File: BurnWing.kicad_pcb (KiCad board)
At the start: 2 copper layers, 50.8 x 22.9 mm, 31 parts, among them J1 Molex_PicoBlade_53398-0471_1x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, J2 Molex_PicoBlade_53047-0610_1x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, J3 feather long, J4 feather short, U1 BTS3405GXUMA1

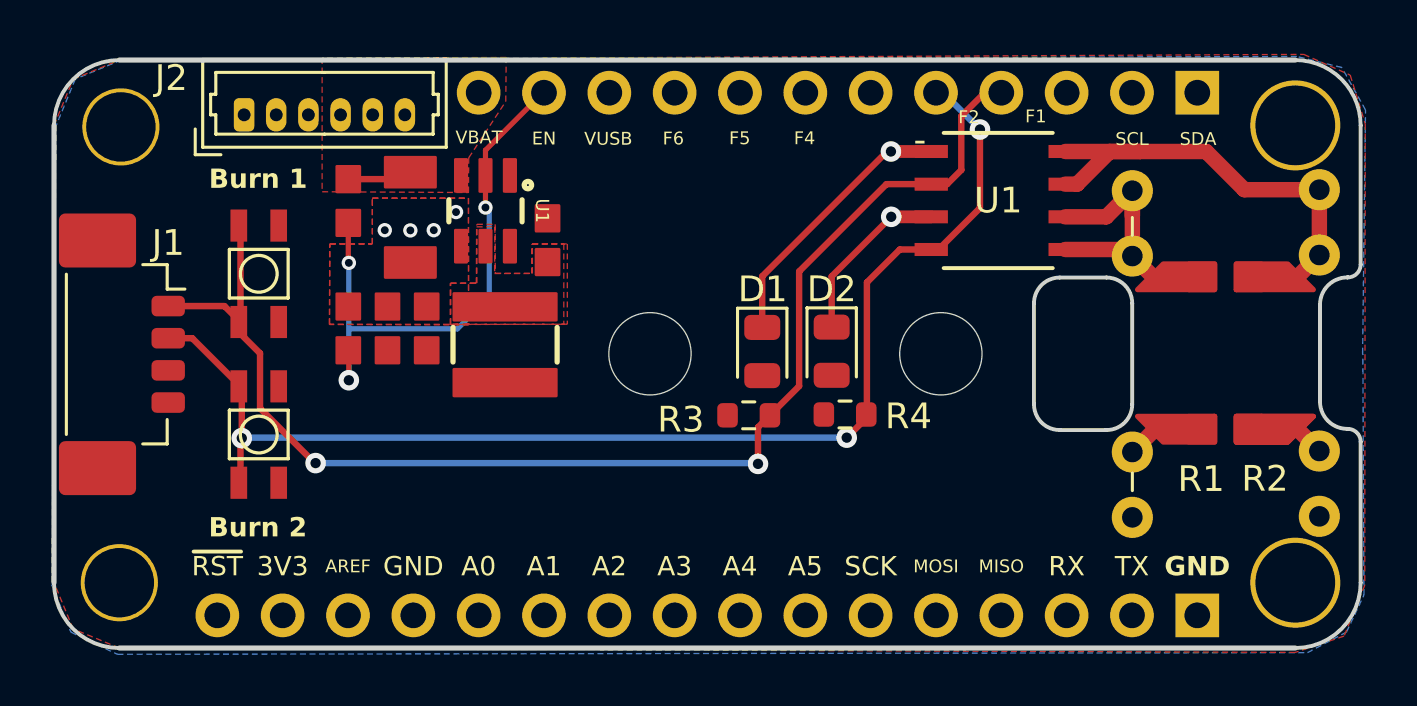
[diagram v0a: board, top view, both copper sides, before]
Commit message: Layout adjustments + added diodes
Added some diodes to prevent backfeeding of test voltage.

Routed remaining two picoblade pins to EN pin on buck reg.
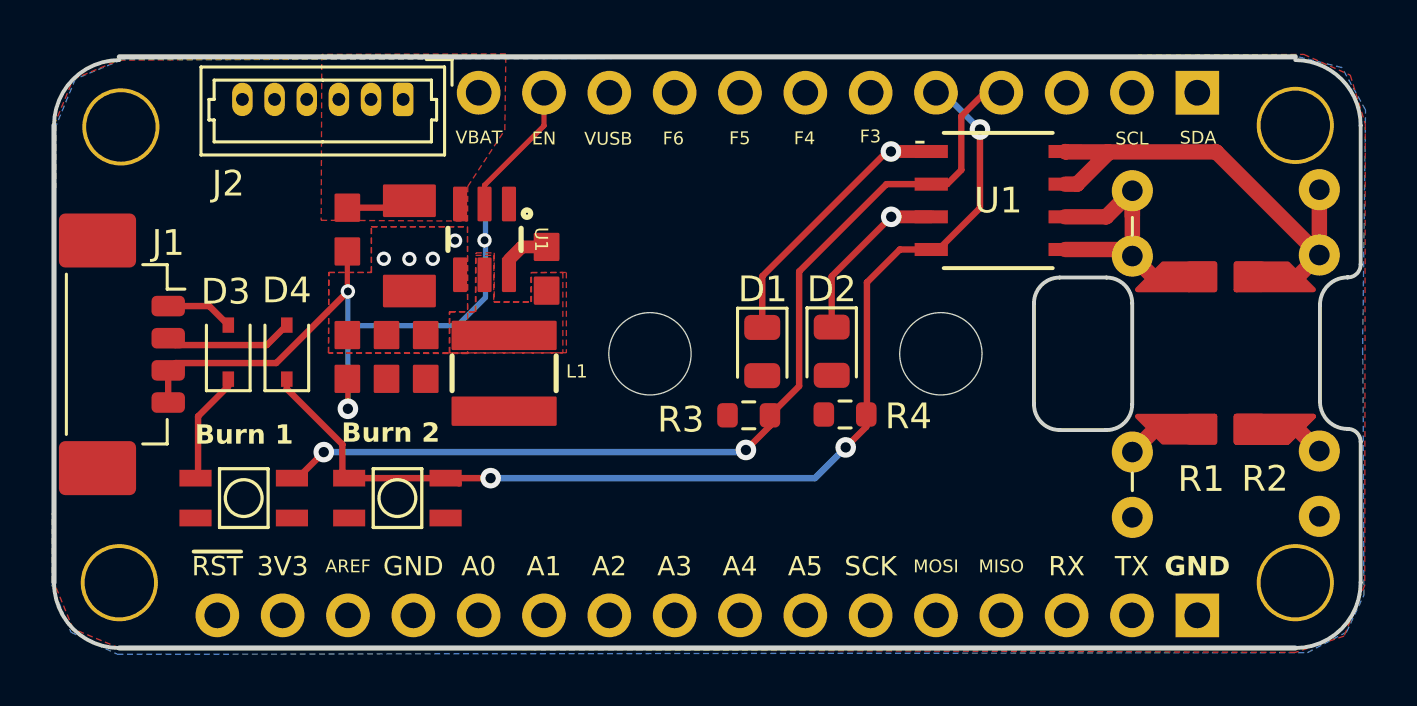
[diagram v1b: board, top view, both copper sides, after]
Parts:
- removed the REF** at (173.7, 105.7)
- removed the REF** at (173.7, 87.9)
- added D3: D_Schottky_Small, Diode_SMD:D_SOD-323, F.Cu at (132.2, 96.8)
- added D4: D_Schottky_Small, Diode_SMD:D_SOD-323, F.Cu at (134.4, 96.8)
- added REF**: MountingHole_2.6mm_M2.5, MountingHole:MountingHole_2.7mm_M2.5, F.Cu at (173.7, 105.7)
- added REF**: MountingHole_2.6mm_M2.5, MountingHole:MountingHole_2.7mm_M2.5, F.Cu at (173.7, 87.9)
- moved Burn 1 8.74 mm to (132.8, 102.4), turned to 180 degrees
- moved J2 6.21 mm to (139.0, 86.9), turned to 180 degrees
- moved Burn 2 5.93 mm to (138.8, 102.4), turned to 180 degrees
- moved C2 1.11 mm to (144.6, 93.5)
- moved C3 1.11 mm to (138.3, 96.9)
- moved C4 1.11 mm to (139.9, 96.9)
- moved R1 1.11 mm to (136.8, 92.0)
- moved R2 1.11 mm to (136.8, 96.9)
- moved U1 1.11 mm to (142.1, 92.4)
- moved C1 1.11 mm to (139.2, 92.6)
- moved L1 1.11 mm to (142.9, 97.6)
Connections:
- J1 pad 3: unconnected-(J1-Pad3) -> EN3V
- J1 pad 4: unconnected-(J1-Pad4) -> EN3V
- J2 pad 1: GND -> Vin
- J2 pad 2: GND -> Vin
- J2 pad 3: GND -> Vin
- J2 pad 4: Vin -> GND
- J2 pad 5: Vin -> GND
- J2 pad 6: Vin -> GND
- U1 pad 6: Net-(R4-Pad2) -> (no net)
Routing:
- net EN3V: track 22.1 -> 31.6 mm
- net IN1: track 51.0 -> 44.9 mm
- net (no net): track 0.00 -> 2.25 mm
- net IN2: track 49.7 -> 48.9 mm
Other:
- board size 50.8 x 22.9 mm -> 50.8 x 23 mm
- board text added: "F3"
- board text removed: "F1"
- board text removed: "F2"
- board text removed: "MountingHole_2.7mm_M2.5"

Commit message: Added couple missing traces
Added missing traces and updated pics/step
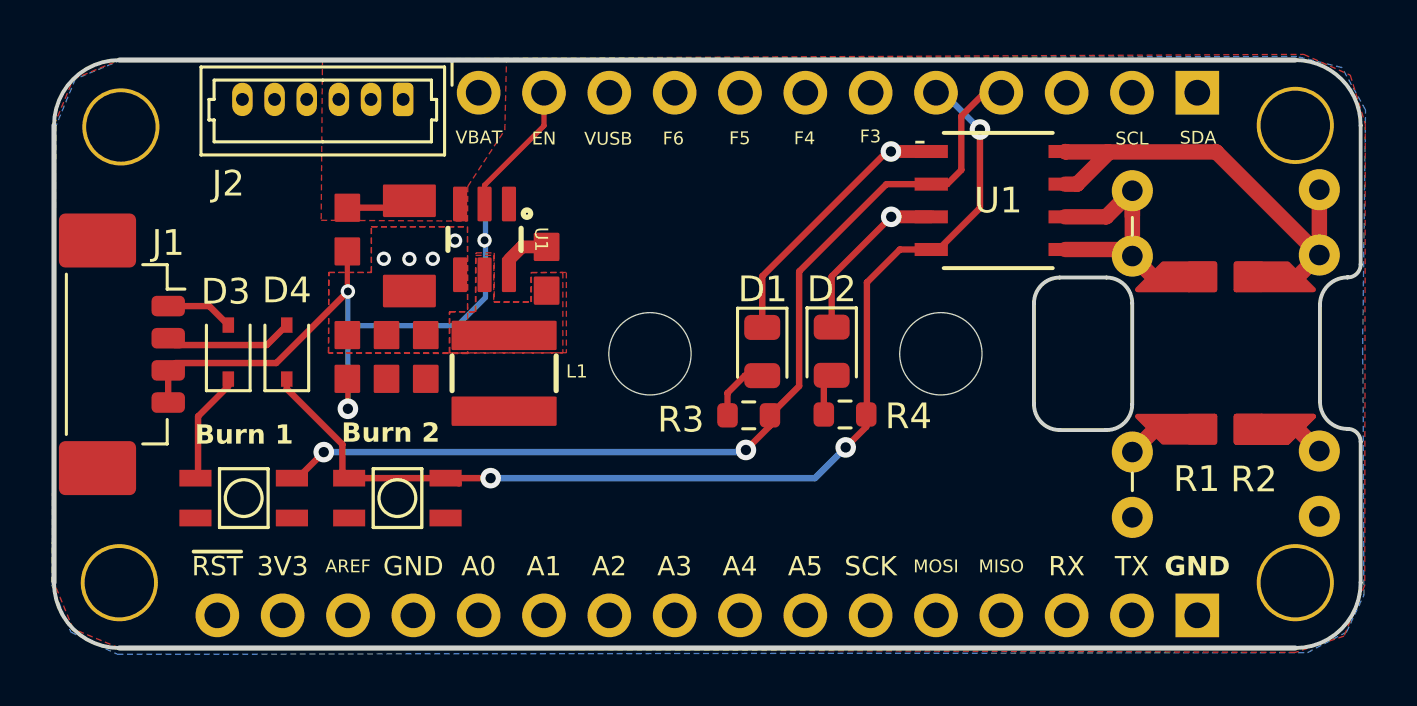
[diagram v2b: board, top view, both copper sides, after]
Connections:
- D1 pad 2: Net-(D1-A) -> (no net)
- D2 pad 2: Net-(D2-A) -> (no net)
- R3 pad 2: Net-(R3-Pad2) -> (no net)
- R4 pad 2: Net-(R4-Pad2) -> (no net)
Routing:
- net (no net): track 2.25 -> 6.40 mm
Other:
- board size 50.8 x 23 mm -> 50.8 x 22.9 mm
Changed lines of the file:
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@@
 	(net 26 "Net-(D1-A)")
 	(net 27 "Net-(D2-A)")
-	(net 28 "Net-(R3-Pad2)")
-	(net 29 "Net-(R4-Pad2)")
-	(net 30 "unconnected-(U2-*INT{slash}SQW-Pad3)")
-	(net 31 "+5V")
+	(net 28 "unconnected-(U2-*INT{slash}SQW-Pad3)")
+	(net 29 "+5V")
 	(footprint "MountingHole:MountingHole_2.7mm_M2.5"
 		(layer "F.Cu")
@@
 			(layers "F.Cu" "F.Paste" "F.Mask")
 			(roundrect_rratio 0.25)
-			(net 26 "Net-(D1-A)")
 			(pinfunction "A")
 			(pintype "passive")
@@
 			(layers "F.Cu" "F.Paste" "F.Mask")
 			(roundrect_rratio 0.25)
-			(net 28 "Net-(R3-Pad2)")
 			(pintype "passive")
 		)
@@
 			(layers "F.Cu" "F.Paste" "F.Mask")
 			(roundrect_rratio 0.09236363636)
-			(net 31 "+5V")
+			(net 29 "+5V")
 			(pinfunction "SOURCE1")
 			(pintype "power_out")
@@
 			(layers "*.Cu" "*.Mask")
 			(remove_unused_layers no)
-			(net 31 "+5V")
+			(net 29 "+5V")
 			(pintype "passive")
 		)
@@
 		(tags "Resistor Axial_DIN0207 series Axial Horizontal pin pitch 7.62mm 0.25W = 1/4W length 6.3mm diameter 2.5mm")
 		(property "Reference" "R2"
-			(at 8.7 2.115 0)
+			(at 8.725 2.545 0)
 			(layer "F.SilkS")
 			(effects
@@
 			(layers "*.Cu" "*.Mask")
 			(remove_unused_layers no)
-			(net 31 "+5V")
+			(net 29 "+5V")
 			(pintype "passive")
 		)
@@
 			(layers "F.Cu" "F.Paste" "F.Mask")
 			(roundrect_rratio 0.0508)
-			(net 31 "+5V")
+			(net 29 "+5V")
 			(solder_mask_margin 0.0635)
 			(zone_connect 2)
@@
 			(layers "F.Cu" "F.Paste" "F.Mask")
 			(roundrect_rratio 0.0508)
-			(net 31 "+5V")
+			(net 29 "+5V")
 			(pintype "passive")
 			(solder_mask_margin 0.0635)
@@
 			(size 0.65 1.25)
 			(layers "F.Cu" "F.Paste" "F.Mask")
-			(net 31 "+5V")
+			(net 29 "+5V")
 			(solder_mask_margin 0.02)
 			(thermal_bridge_angle 0)
@@
 			(size 0.65 1.25)
 			(layers "F.Cu" "F.Paste" "F.Mask")
-			(net 31 "+5V")
+			(net 29 "+5V")
 			(solder_mask_margin 0.02)
 			(thermal_bridge_angle 0)
@@
 			(layers "F.Cu" "F.Paste" "F.Mask")
 			(roundrect_rratio 0.25)
-			(net 29 "Net-(R4-Pad2)")
 			(pintype "passive")
 		)
@@
 			(layers "*.Cu" "*.Mask")
 			(remove_unused_layers no)
-			(net 31 "+5V")
+			(net 29 "+5V")
 			(zone_connect 1)
 		)
@@
 			(size 0.65 1.25)
 			(layers "F.Cu" "F.Paste" "F.Mask")
-			(net 31 "+5V")
+			(net 29 "+5V")
 			(solder_mask_margin 0.02)
 			(thermal_bridge_angle 0)
@@
 			(size 0.65 1.25)
 			(layers "F.Cu" "F.Paste" "F.Mask")
-			(net 31 "+5V")
+			(net 29 "+5V")
 			(solder_mask_margin 0.02)
 			(thermal_bridge_angle 0)
@@
 			(layers "F.Cu" "F.Paste" "F.Mask")
 			(roundrect_rratio 0.25)
-			(net 27 "Net-(D2-A)")
 			(pinfunction "A")
 			(pintype "passive")
@@
 			(size 1 1)
 			(layers "F.Cu" "F.Paste" "F.Mask")
-			(net 31 "+5V")
+			(net 29 "+5V")
 			(pintype "passive")
 			(thermal_bridge_angle 90)
@@
 		(tags "Resistor Axial_DIN0309 series Axial Horizontal pin pitch 12.7mm 0.5W = 1/2W length 9mm diameter 3.2mm")
 		(property "Reference" "R1"
-			(at 11.21 -2.675 0)
+			(at 11.21 -2.5 0)
 			(layer "F.SilkS")
 			(effects
@@
 			(layers "*.Cu" "*.Mask")
 			(remove_unused_layers no)
-			(net 31 "+5V")
+			(net 29 "+5V")
 			(pintype "passive")
 		)
@@
 			(size 1 1)
 			(layers "F.Cu" "F.Paste" "F.Mask")
-			(net 31 "+5V")
+			(net 29 "+5V")
 			(pintype "passive")
 			(thermal_bridge_angle 90)
@@
 			(layers "F.Cu" "F.Paste" "F.Mask")
 			(roundrect_rratio 0.04444444444)
-			(net 31 "+5V")
+			(net 29 "+5V")
 			(solder_mask_margin 0.0635)
 			(zone_connect 2)
@@
 			(layers "*.Cu" "*.Mask")
 			(remove_unused_layers no)
-			(net 30 "unconnected-(U2-*INT{slash}SQW-Pad3)")
+			(net 28 "unconnected-(U2-*INT{slash}SQW-Pad3)")
 			(pinfunction "Pin_7")
 			(pintype "passive")
@@
 			(layers "*.Cu" "*.Mask")
 			(remove_unused_layers no)
-			(net 31 "+5V")
+			(net 29 "+5V")
 			(pinfunction "Pin_10")
 			(pintype "passive")
@@
 	)
 	(gr_line
-		(start 127.94 85.275)
-		(end 173.66 85.275)
+		(start 127.94 85.4)
+		(end 173.66 85.4)
 		(stroke
 			(width 0.2)
@@
 	)
 	(segment
+		(start 155.33 99.18)
+		(end 155.33 97.9625)
+		(width 0.25)
+		(layer "F.Cu")
+		(net 0)
+	)
+	(segment
 		(start 143.088 93.7463)
 		(end 143.088 93.167)
@@
 	)
 	(segment
+		(start 155.33 97.9625)
+		(end 155.635 97.6575)
+		(width 0.25)
+		(layer "F.Cu")
+		(net 0)
+	)
+	(segment
+		(start 152.259998 97.670002)
+		(end 152.935 97.670002)
+		(width 0.25)
+		(layer "F.Cu")
+		(net 0)
+	)
+	(segment
 		(start 143.088 93.167)
 		(end 143.5908 92.6642)
@@
 	)
 	(segment
+		(start 151.585 99.2125)
+		(end 151.585 98.345)
+		(width 0.25)
+		(layer "F.Cu")
+		(net 0)
+	)
+	(segment
+		(start 151.585 98.345)
+		(end 152.259998 97.670002)
+		(width 0.25)
+		(layer "F.Cu")
+		(net 0)
+	)
+	(segment
 		(start 143.5908 92.6642)
 		(end 144.551 92.6642)
@@
 		(width 0.25)
 		(layer "B.Cu")
-		(net 30)
+		(net 28)
 	)
 	(segment
@@
 		(width 0.25)
 		(layer "F.Cu")
-		(net 31)
+		(net 29)
 	)
 	(segment
@@
 		(width 0.6)
 		(layer "F.Cu")
-		(net 31)
+		(net 29)
 	)
 	(segment
@@
 		(width 0.6)
 		(layer "F.Cu")
-		(net 31)
+		(net 29)
 	)
 	(segment
@@
 		(width 0.6)
 		(layer "F.Cu")
-		(net 31)
+		(net 29)
 	)
 	(segment
@@
 		(width 0.6)
 		(layer "F.Cu")
-		(net 31)
+		(net 29)
 	)
 	(zone
@@
 		(polygon
 			(pts
-				(xy 135.787 91.6302) (xy 141.477 91.6602) (xy 141.487 90.3102) (xy 142.927 88.1202) (xy 142.968 85.1602)
-				(xy 135.812 85.1802)
+				(xy 135.787 91.6302) (xy 141.477 91.6602) (xy 141.487 90.3102) (xy 142.927 88.1202) (xy 142.993 85.3602)
+				(xy 135.837 85.3802)
 			)
 		)
 	)
 	(zone
-		(net 31)
+		(net 29)
 		(net_name "+5V")
 		(layer "F.Cu")
@@
 	)
 	(zone
-		(net 31)
+		(net 29)
 		(net_name "+5V")
 		(layer "F.Cu")
